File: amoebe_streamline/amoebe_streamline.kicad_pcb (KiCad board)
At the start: 2 copper layers, 19.1 x 19 mm, 11 parts, among them J1 Conn_01x02_Pin, J2 Conn_01x02_Pin, J3 Conn_01x02_Pin, J4 Conn_01x02_Pin, J5 Conn_01x01_Pin, J6 Conn_01x01_Pin

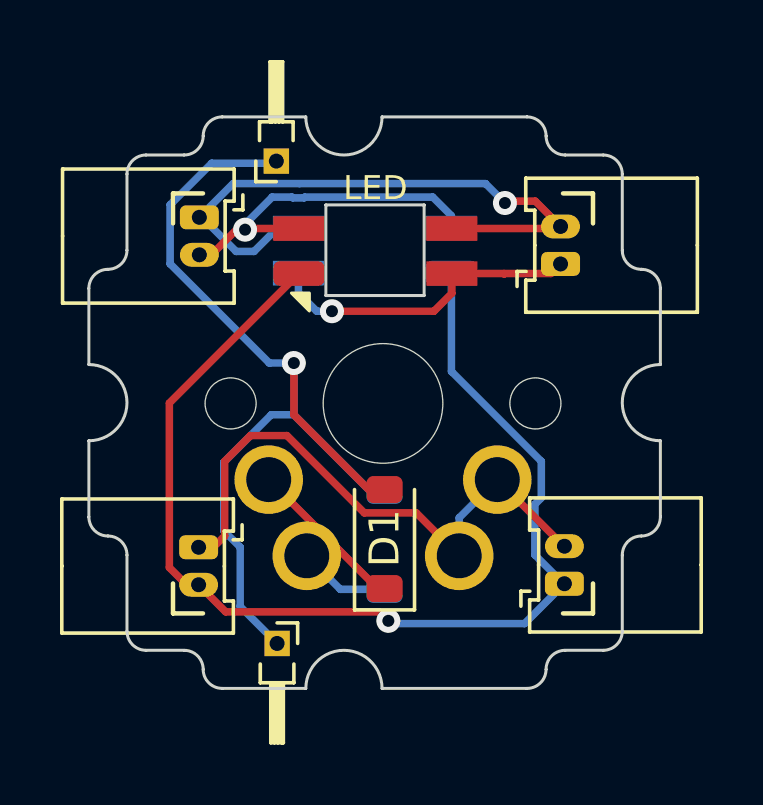
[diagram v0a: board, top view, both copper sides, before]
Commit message: Fixes data lines for LED
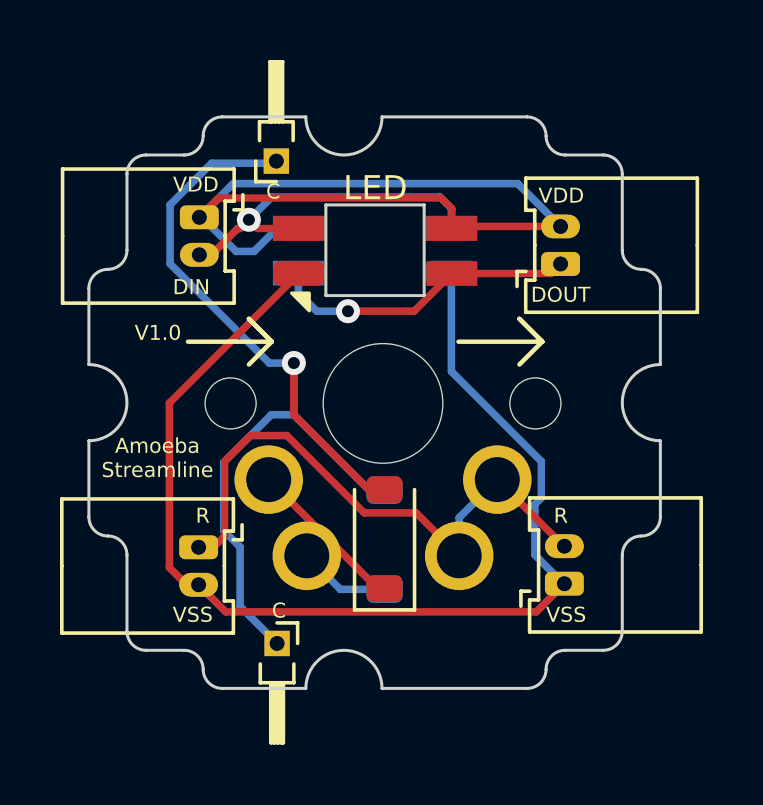
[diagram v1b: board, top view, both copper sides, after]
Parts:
- renumbered LED to D2
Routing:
- net /VDD: track 20.8 -> 30.4 mm, vias 1 -> 0
- net /VSS: track 38.2 -> 37.9 mm, vias 1 -> 0
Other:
- board text added: "Amoeba Streamline"
- board text added: "C"
- board text added: "DIN"
- board text added: "DOUT"
- board text added: "R"
- board text added: "V1.0"
- board text added: "VDD"
- board text added: "VSS"

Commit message: Added 3d files
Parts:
- renumbered LED to r
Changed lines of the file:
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@@
     (pad "2" thru_hole circle (at 3.81 -2.54 180) (size 2.286 2.286) (drill 1.4986) (layers "*.Cu" "*.Mask")
       (net 1 "Net-(D1-A)") (pintype "passive"))
+    (model "${KIPRJMOD}/asm_mx_asm_PLATE.stp"
+      (offset (xyz -0.3 0.3 -6))
+      (scale (xyz 1 1 1))
+      (rotate (xyz 0 0 90))
+    )
   )
   (footprint "Connector_Molex:Molex_PicoBlade_53048-0210_1x02_P1.25mm_Horizontal" (layer "F.Cu")
@@
       (rotate (xyz 0 0 0))
     )
+    (model "${KIPRJMOD}/530480260.stp"
+      (offset (xyz 0.6 -5.5 0))
+      (scale (xyz 1 1 1))
+      (rotate (xyz 0 0 0))
+    )
   )
   (footprint "Diode_SMD:D_SOD-123" (layer "F.Cu")
@@
     (property "Sheetname" "LED")
     (attr through_hole)
-    (fp_text reference "LED" (at 0 2.1 unlocked) (layer "F.SilkS")
+    (fp_text reference "r" (at 0 2.1 unlocked) (layer "F.SilkS") hide
         (effects (font (size 0.8 0.8) (thickness 0.15)))
     )
@@
     (pad "4" smd rect (at 2.55 0.75 180) (size 1.7 0.82) (layers "F.Cu" "F.Paste" "F.Mask")
       (net 6 "/DIN") (pinfunction "DIN") (pintype "input"))
-    (model "/Users/danny/syncproj/kicad-libs/footprints/Keebio-Parts.pretty/3dmodels/SK6812MINI-E v1.step"
-      (offset (xyz 0 0 0))
-      (scale (xyz 1 1 1))
-      (rotate (xyz 90 0 0))
+    (model "${KIPRJMOD}/LED_SK6812MINI-E.step"
+      (offset (xyz 0 -5 -1.77))
+      (scale (xyz 1 1 1))
+      (rotate (xyz 180 0 0))
     )
   )
@@
       (rotate (xyz 0 0 0))
     )
+    (model "${KIPRJMOD}/530480260.stp"
+      (offset (xyz 0.6 -5.5 0))
+      (scale (xyz 1 1 1))
+      (rotate (xyz 0 0 0))
+    )
   )
   (footprint "Connector_Molex:Molex_PicoBlade_53048-0210_1x02_P1.25mm_Horizontal" (layer "F.Cu")
@@
       (rotate (xyz 0 0 0))
     )
+    (model "${KIPRJMOD}/530480260.stp"
+      (offset (xyz 0.6 -5.5 0))
+      (scale (xyz 1 1 1))
+      (rotate (xyz 0 0 0))
+    )
   )
   (footprint "Connector_PinHeader_1.00mm:PinHeader_1x01_P1.00mm_Horizontal" (layer "F.Cu")
@@
       (rotate (xyz 0 0 0))
     )
+    (model "${KIPRJMOD}/530480260.stp"
+      (offset (xyz 0.6 -5.5 0))
+      (scale (xyz 1 1 1))
+      (rotate (xyz 0 0 0))
+    )
   )
   (footprint "Diode_SMD:D_SOD-123" (layer "B.Cu")
@@
     (property "Sheetname" "Switch")
     (attr smd)
-    (fp_text reference "D1" (at -0.0752 0.0254 90) (layer "B.SilkS") hide
+    (fp_text reference "D1" (at -0.0752 0.0254 -90) (layer "B.SilkS") hide
         (effects (font (size 1 1) (thickness 0.15)) (justify mirror))
     )
-    (fp_text value "1N4148W-7-F" (at 0 -2.1 90) (layer "B.Fab")
+    (fp_text value "1N4148W-7-F" (at 0 -2.1 -90) (layer "B.Fab")
         (effects (font (size 1 1) (thickness 0.15)) (justify mirror))
     )
-    (fp_text user "${REFERENCE}" (at 0 2 90) (layer "B.Fab")
+    (fp_text user "${REFERENCE}" (at 0 2 -90) (layer "B.Fab")
         (effects (font (size 1 1) (thickness 0.15)) (justify mirror))
     )
@@
     (pad "2" smd roundrect (at 1.65 0 90) (size 0.9 1.2) (layers "B.Cu" "B.Paste" "B.Mask") (roundrect_rratio 0.25)
       (net 2 "/C") (pinfunction "K") (pintype "passive"))
-    (model "${KICAD6_3DMODEL_DIR}/Diode_SMD.3dshapes/D_SOD-123.wrl"
+    (model "${KICAD6_3DMODEL_DIR}/Diode_SMD.3dshapes/D_SOD-123.wrl" hide
       (offset (xyz 0 0 0))
       (scale (xyz 1 1 1))
@@
     (property "Sheetname" "LED")
     (attr through_hole)
-    (fp_text reference "D2" (at 0 -2.1 unlocked) (layer "B.SilkS")
+    (fp_text reference "D2" (at 0 -2.1 unlocked) (layer "B.SilkS") hide
         (effects (font (size 0.8 0.8) (thickness 0.15)) (justify mirror))
     )

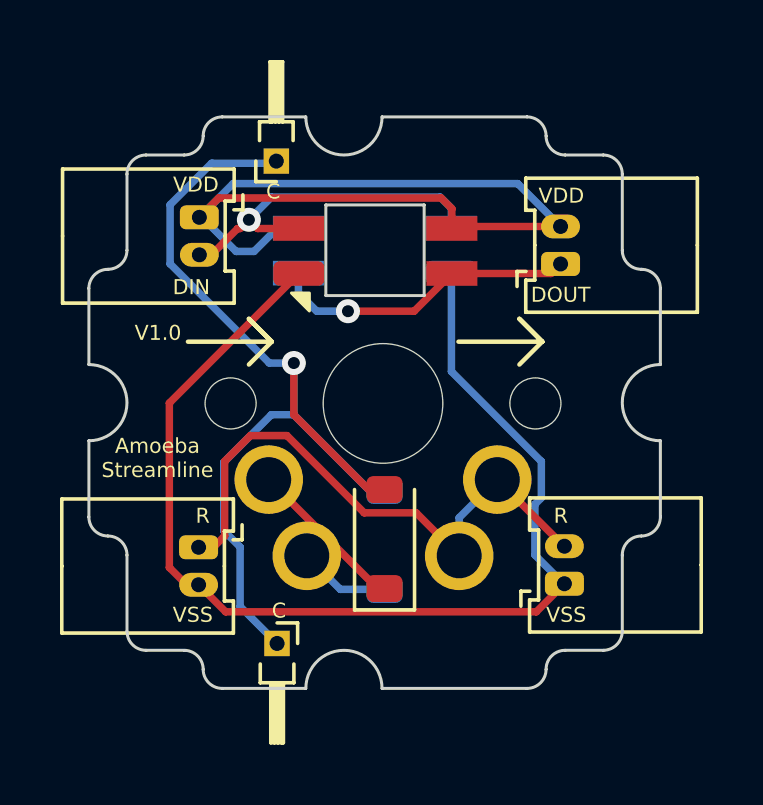
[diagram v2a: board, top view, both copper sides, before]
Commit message: version 1.2 with additional ground pins
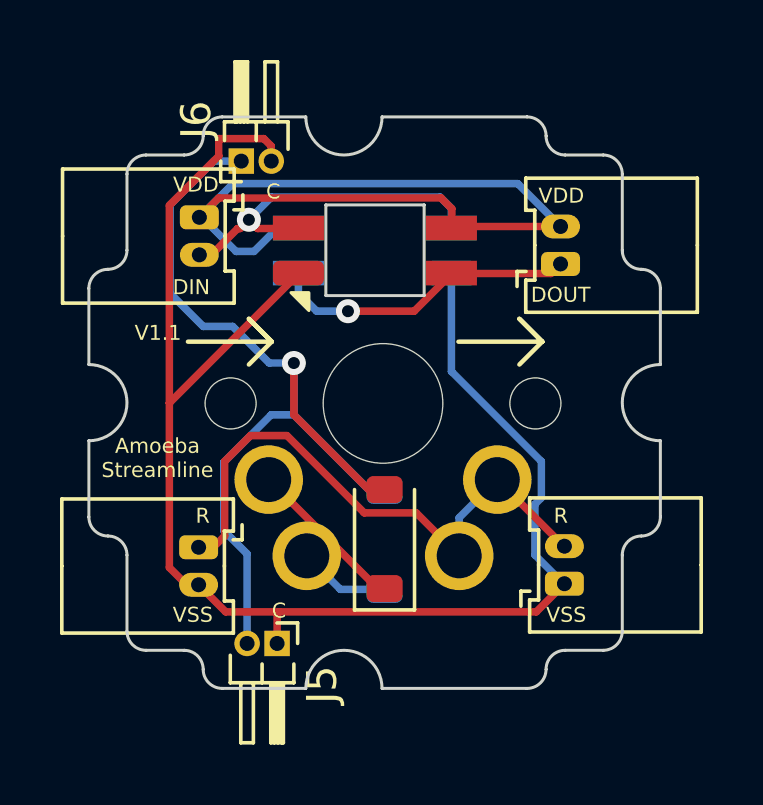
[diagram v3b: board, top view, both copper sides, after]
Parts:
- removed r: SK6812MINI_E, CustomFootprints:SK6812-MINI-E
- added D2: SK6812MINI_E, CustomFootprints:SK6812-MINI-E, F.Cu at (142.9, 95.3)
- J5, J6: value Conn_01x01_Pin -> Conn_01x02_Pin; footprint Connector_PinHeader_1.00mm:PinHeader_1x01_P1.00mm_Horizontal -> Connector_PinHeader_1.00mm:PinHeader_1x02_P1.00mm_Horizontal
- moved J6 1.17 mm to (138.4, 92.3)
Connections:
- J5 pad 1: /C -> /VSS
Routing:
- net /VSS: track 37.9 -> 50.9 mm
- net /C: track 32.4 -> 31.4 mm
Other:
- board text added: "V1.1"
- board text removed: "V1.0"
